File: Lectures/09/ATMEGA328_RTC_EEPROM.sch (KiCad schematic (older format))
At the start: 19 parts, among them U1 ATmega328P-AU, U2 24LC1025, U3 24LC1025, U4 DS1337S+, Y1 Crystal 16MHz, Y2 Crystal 32MHz

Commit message: Included decoupling capacitors
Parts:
- added C10, C4, C5, C6, C7, C8, C9: 100nF, Capacitor_SMD:C_0603_1608Metric_Pad1.08x0.95mm_HandSolder, symbol Device:C
- C1, C2: footprint Capacitor_SMD:C_0805_2012Metric_Pad1.18x1.45mm_HandSolder -> Capacitor_SMD:C_0603_1608Metric_Pad1.08x0.95mm_HandSolder
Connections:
- net labels removed: GNDPWR
- wire segments 107 -> 125
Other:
- moved on the sheet: BT1, C1, C2, D1, R3, U2, Y1

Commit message: Reverse Input Voltage Polarity Protection
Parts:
- removed D2, D3: D, Diode_SMD:D_0805_2012Metric_Pad1.15x1.40mm_HandSolder, symbol Device:D
- added D2, D3: MBR0520LT, Diode_SMD:D_SOD-123, symbol Diode:MBR0520LT
- added Q1: IRLML6401, Package_TO_SOT_SMD:SOT-23, symbol Transistor_FET:IRLML6401
- BT1: value CR1225 -> CR2032; footprint Battery:Battery_CR1225 -> Battery:BatteryHolder_Keystone_1058_1x2032
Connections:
- wire segments 125 -> 123
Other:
- moved on the sheet: BT1, BT2, C3
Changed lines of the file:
@@
 $EndDescr
-$Comp
-L Device:Battery BT2
-U 1 1 60094422
-P 10500 2800
-F 0 "BT2" H 10608 2846 50  0000 L CNN
-F 1 "3.3V" H 10608 2755 50  0000 L CNN
-F 2 "Connector_PinHeader_2.54mm:PinHeader_1x02_P2.54mm_Vertical" V 10500 2860 50  0001 C CNN
-F 3 "~" V 10500 2860 50  0001 C CNN
-	1    10500 2800
-	1    0    0    -1
-$EndComp
-$Comp
-L Device:CP C3
-U 1 1 60096B17
-P 9750 2850
-F 0 "C3" H 9868 2896 50  0000 L CNN
-F 1 "10uF" H 9868 2805 50  0000 L CNN
-F 2 "Capacitor_SMD:C_0805_2012Metric_Pad1.18x1.45mm_HandSolder" H 9788 2700 50  0001 C CNN
-F 3 "~" H 9750 2850 50  0001 C CNN
-	1    9750 2850
-	1    0    0    -1
-$EndComp
 $Comp
 L Custom_RTC_Library:DS1337S+_v1 U4
@@
 	1    8000 2925
 	1    0    0    -1
-$EndComp
-$Comp
-L Device:D D2
-U 1 1 600D352F
-P 7750 1600
-F 0 "D2" V 7796 1520 50  0000 R CNN
-F 1 "D" V 7705 1520 50  0000 R CNN
-F 2 "Diode_SMD:D_0805_2012Metric_Pad1.15x1.40mm_HandSolder" H 7750 1600 50  0001 C CNN
-F 3 "~" H 7750 1600 50  0001 C CNN
-	1    7750 1600
-	0    -1   -1   0
-$EndComp
-$Comp
-L Device:D D3
-U 1 1 600D3E15
-P 8250 1600
-F 0 "D3" V 8296 1520 50  0000 R CNN
-F 1 "D" V 8205 1520 50  0000 R CNN
-F 2 "Diode_SMD:D_0805_2012Metric_Pad1.15x1.40mm_HandSolder" H 8250 1600 50  0001 C CNN
-F 3 "~" H 8250 1600 50  0001 C CNN
-	1    8250 1600
-	0    -1   -1   0
 $EndComp
 Text Label 8750 4600 2    50   ~ 0
@@
 	8750 5750 9000 5750
 Wire Wire Line
-	8750 5875 8875 5875
-Wire Wire Line
-	8875 6000 8875 5875
-Connection ~ 8875 5875
-Wire Wire Line
-	8875 5875 9000 5875
-Wire Wire Line
 	10250 4600 10500 4600
 Wire Wire Line
@@
 Wire Wire Line
 	8600 3175 8750 3175
-Text Label 7750 1250 0    50   ~ 0
+Text Label 7625 1250 0    50   ~ 0
 Vcc
 $Comp
 L Device:Battery_Cell BT1
 U 1 1 600D5613
-P 8750 1450
-F 0 "BT1" H 8868 1546 50  0000 L CNN
-F 1 "CR1225" H 8868 1455 50  0000 L CNN
-F 2 "Battery:Battery_CR1225" V 8750 1510 50  0001 C CNN
-F 3 "~" V 8750 1510 50  0001 C CNN
-	1    8750 1450
-	1    0    0    -1
-$EndComp
-Wire Wire Line
-	7750 1750 7750 1850
-Wire Wire Line
-	8250 1750 8250 1850
-Wire Wire Line
-	7750 1250 7750 1450
-Wire Wire Line
-	8250 1450 8250 1250
-Wire Wire Line
-	8250 1250 8750 1250
-Wire Wire Line
-	8750 1750 8750 1550
+P 8750 1525
+F 0 "BT1" H 8868 1621 50  0000 L CNN
+F 1 "CR2032" H 8868 1530 50  0000 L CNN
+F 2 "Battery:BatteryHolder_Keystone_1058_1x2032" V 8750 1585 50  0001 C CNN
+F 3 "~" V 8750 1585 50  0001 C CNN
+	1    8750 1525
+	1    0    0    -1
+$EndComp
 $Comp
 L Memory_EEPROM:24LC1025 U3
@@
 Wire Wire Line
 	5550 2550 5550 2500
-Wire Wire Line
-	9750 3000 9750 3125
-Wire Wire Line
-	10500 3125 10500 3000
-Text Label 10125 2250 0    50   ~ 0
+Text Label 6075 5750 0    50   ~ 0
 Vcc
-Wire Wire Line
-	9750 2700 9750 2500
-Wire Wire Line
-	9750 2500 10125 2500
-Wire Wire Line
-	10500 2500 10500 2600
-Wire Wire Line
-	10125 2250 10125 2375
-Connection ~ 10125 2500
-Wire Wire Line
-	10125 2500 10500 2500
 $Comp
 L Device:LED D1
@@
 NoConn ~ 2400 3475
 NoConn ~ 2400 3575
-$Comp
-L power:PWR_FLAG #FLG0101
-U 1 1 601BAE2E
-P 10125 2375
-F 0 "#FLG0101" H 10125 2450 50  0001 C CNN
-F 1 "PWR_FLAG" V 10125 2503 50  0000 L CNN
-F 2 "" H 10125 2375 50  0001 C CNN
-F 3 "~" H 10125 2375 50  0001 C CNN
-	1    10125 2375
-	0    1    1    0
-$EndComp
-Connection ~ 10125 2375
-Wire Wire Line
-	10125 2375 10125 2500
 Wire Notes Line
 	4750 1000 6250 1000
 Wire Notes Line
 	6500 1000 9250 1000
-Wire Notes Line
-	9500 1000 11000 1000
 Text Notes 6500 975  0    50   ~ 0
 N3 - Clock/Calendar and Backup Battery
@@
 Text Notes 625  975  0    50   ~ 0
 N1 - Atmega328P with Oscillator
-Text Notes 9500 975  0    50   ~ 0
+Text Notes 4750 5225 0    50   ~ 0
 N4 - External Battery Terminal
 Wire Notes Line
 	6500 4000 9250 4000
 Wire Notes Line
-	9500 4000 11000 4000
-Wire Notes Line
 	6500 4000 6500 1000
 Wire Notes Line
 	9250 1000 9250 4000
-Wire Notes Line
-	9500 4000 9500 1000
-Wire Notes Line
-	11000 1000 11000 4000
 Wire Notes Line
 	8250 4250 8250 6250
@@
 $EndComp
 $Comp
-L power:GND #PWR014
-U 1 1 600D5E04
-P 8875 6000
-F 0 "#PWR014" H 8875 5750 50  0001 C CNN
-F 1 "GND" H 8880 5827 50  0000 C CNN
-F 2 "" H 8875 6000 50  0001 C CNN
-F 3 "" H 8875 6000 50  0001 C CNN
-	1    8875 6000
-	1    0    0    -1
-$EndComp
-$Comp
 L power:GND #PWR015
 U 1 1 600D67BE
-P 10125 3325
-F 0 "#PWR015" H 10125 3075 50  0001 C CNN
-F 1 "GND" H 10130 3152 50  0000 C CNN
-F 2 "" H 10125 3325 50  0001 C CNN
-F 3 "" H 10125 3325 50  0001 C CNN
-	1    10125 3325
+P 5000 6325
+F 0 "#PWR015" H 5000 6075 50  0001 C CNN
+F 1 "GND" H 5005 6152 50  0000 C CNN
+F 2 "" H 5000 6325 50  0001 C CNN
+F 3 "" H 5000 6325 50  0001 C CNN
+	1    5000 6325
 	1    0    0    -1
 $EndComp
@@
 L power:GND #PWR013
 U 1 1 600D7A06
-P 8750 1750
-F 0 "#PWR013" H 8750 1500 50  0001 C CNN
-F 1 "GND" H 8755 1577 50  0000 C CNN
-F 2 "" H 8750 1750 50  0001 C CNN
-F 3 "" H 8750 1750 50  0001 C CNN
-	1    8750 1750
+P 8750 1725
+F 0 "#PWR013" H 8750 1475 50  0001 C CNN
+F 1 "GND" H 8755 1552 50  0000 C CNN
+F 2 "" H 8750 1725 50  0001 C CNN
+F 3 "" H 8750 1725 50  0001 C CNN
+	1    8750 1725
 	1    0    0    -1
 $EndComp
@@
 	1    0    0    -1
 $EndComp
-Text Label 10225 3225 0    50   ~ 0
+Text Label 6075 6250 0    50   ~ 0
 GND
-Wire Wire Line
-	9750 3125 10125 3125
-Wire Wire Line
-	10125 3225 10125 3125
-Wire Wire Line
-	10125 3225 10225 3225
-Connection ~ 10125 3125
-Wire Wire Line
-	10125 3125 10500 3125
-Wire Wire Line
-	10125 3325 10125 3225
-Connection ~ 10125 3225
 $Comp
 L power:GND #PWR07
@@
 Text Label 5550 3250 0    50   ~ 0
 Vcc
-Wire Wire Line
-	7750 1850 8000 1850
 $Comp
 L Device:C C10
@@
 Wire Wire Line
 	8000 2325 8000 2175
-Connection ~ 8000 1850
-Wire Wire Line
-	8000 1850 8250 1850
 Wire Wire Line
 	7900 2175 8000 2175
@@
 Wire Notes Line
 	4750 1000 4750 5000
+Wire Wire Line
+	7625 1850 8000 1850
+Wire Wire Line
+	8000 1850 8375 1850
+Connection ~ 8000 1850
+Wire Wire Line
+	8375 1450 8375 1250
+Wire Wire Line
+	8375 1250 8750 1250
+Wire Wire Line
+	8750 1250 8750 1325
+Wire Wire Line
+	8750 1725 8750 1625
+$Comp
+L Diode:MBR0520LT D3
+U 1 1 600C40F8
+P 8375 1600
+F 0 "D3" V 8400 1925 50  0000 R CNN
+F 1 "MBR0520LT" V 8325 2100 50  0000 R CNN
+F 2 "Diode_SMD:D_SOD-123" H 8375 1425 50  0001 C CNN
+F 3 "http://www.onsemi.com/pub_link/Collateral/MBR0520LT1-D.PDF" H 8375 1600 50  0001 C CNN
+	1    8375 1600
+	0    -1   -1   0
+$EndComp
+Wire Wire Line
+	8375 1850 8375 1750
+$Comp
+L Diode:MBR0520LT D2
+U 1 1 600AFB22
+P 7625 1600
+F 0 "D2" V 7650 1925 50  0000 R CNN
+F 1 "MBR0520LT" V 7575 2100 50  0000 R CNN
+F 2 "Diode_SMD:D_SOD-123" H 7625 1425 50  0001 C CNN
+F 3 "http://www.onsemi.com/pub_link/Collateral/MBR0520LT1-D.PDF" H 7625 1600 50  0001 C CNN
+	1    7625 1600
+	0    -1   -1   0
+$EndComp
+Wire Wire Line
+	7625 1450 7625 1250
+Wire Wire Line
+	7625 1850 7625 1750
+Wire Wire Line
+	8750 5875 9000 5875
+$Comp
+L Transistor_FET:IRLML6401 Q1
+U 1 1 600E5C2A
+P 5500 5850
+F 0 "Q1" V 5842 5850 50  0000 C CNN
+F 1 "IRLML6401" V 5751 5850 50  0000 C CNN
+F 2 "Package_TO_SOT_SMD:SOT-23" H 5700 5775 50  0001 L CIN
+F 3 "https://www.infineon.com/dgdl/irlml6401pbf.pdf?fileId=5546d462533600a401535668b96d2634" H 5500 5850 50  0001 L CNN
+	1    5500 5850
+	0    -1   -1   0
+$EndComp
+$Comp
+L Device:Battery BT2
+U 1 1 60094422
+P 5000 5950
+F 0 "BT2" H 5108 5996 50  0000 L CNN
+F 1 "3.3V" H 5108 5905 50  0000 L CNN
+F 2 "Connector_PinHeader_2.54mm:PinHeader_1x02_P2.54mm_Vertical" V 5000 6010 50  0001 C CNN
+F 3 "~" V 5000 6010 50  0001 C CNN
+	1    5000 5950
+	1    0    0    -1
+$EndComp
+$Comp
+L power:PWR_FLAG #FLG0101
+U 1 1 601BAE2E
+P 6000 5825
+F 0 "#FLG0101" H 6000 5900 50  0001 C CNN
+F 1 "PWR_FLAG" V 6000 5953 50  0000 L CNN
+F 2 "" H 6000 5825 50  0001 C CNN
+F 3 "~" H 6000 5825 50  0001 C CNN
+	1    6000 5825
+	0    1    1    0
+$EndComp
+Wire Wire Line
+	5300 5750 5000 5750
+$Comp
+L Device:CP C3
+U 1 1 60096B17
+P 6000 6025
+F 0 "C3" H 6118 6071 50  0000 L CNN
+F 1 "10uF" H 6118 5980 50  0000 L CNN
+F 2 "Capacitor_SMD:C_0805_2012Metric_Pad1.18x1.45mm_HandSolder" H 6038 5875 50  0001 C CNN
+F 3 "~" H 6000 6025 50  0001 C CNN
+	1    6000 6025
+	1    0    0    -1
+$EndComp
+Wire Wire Line
+	5000 6150 5000 6250
+Wire Wire Line
+	5000 6250 5500 6250
+Wire Wire Line
+	5500 6050 5500 6250
+Connection ~ 5500 6250
+Wire Wire Line
+	5000 6325 5000 6250
+Connection ~ 5000 6250
+Wire Wire Line
+	5700 5750 6000 5750
+Wire Wire Line
+	5500 6250 6000 6250
+Wire Wire Line
+	6000 6175 6000 6250
+Connection ~ 6000 6250
+Wire Wire Line
+	6000 6250 6075 6250
+Wire Wire Line
+	6000 5875 6000 5825
+Connection ~ 6000 5750
+Wire Wire Line
+	6000 5750 6075 5750
+Connection ~ 6000 5825
+Wire Wire Line
+	6000 5825 6000 5750
+Wire Notes Line
+	4750 5250 4750 6750
+Wire Notes Line
+	4750 6750 6750 6750
+Wire Notes Line
+	6750 6750 6750 5250
+Wire Notes Line
+	6750 5250 4750 5250
 $EndSCHEMATC

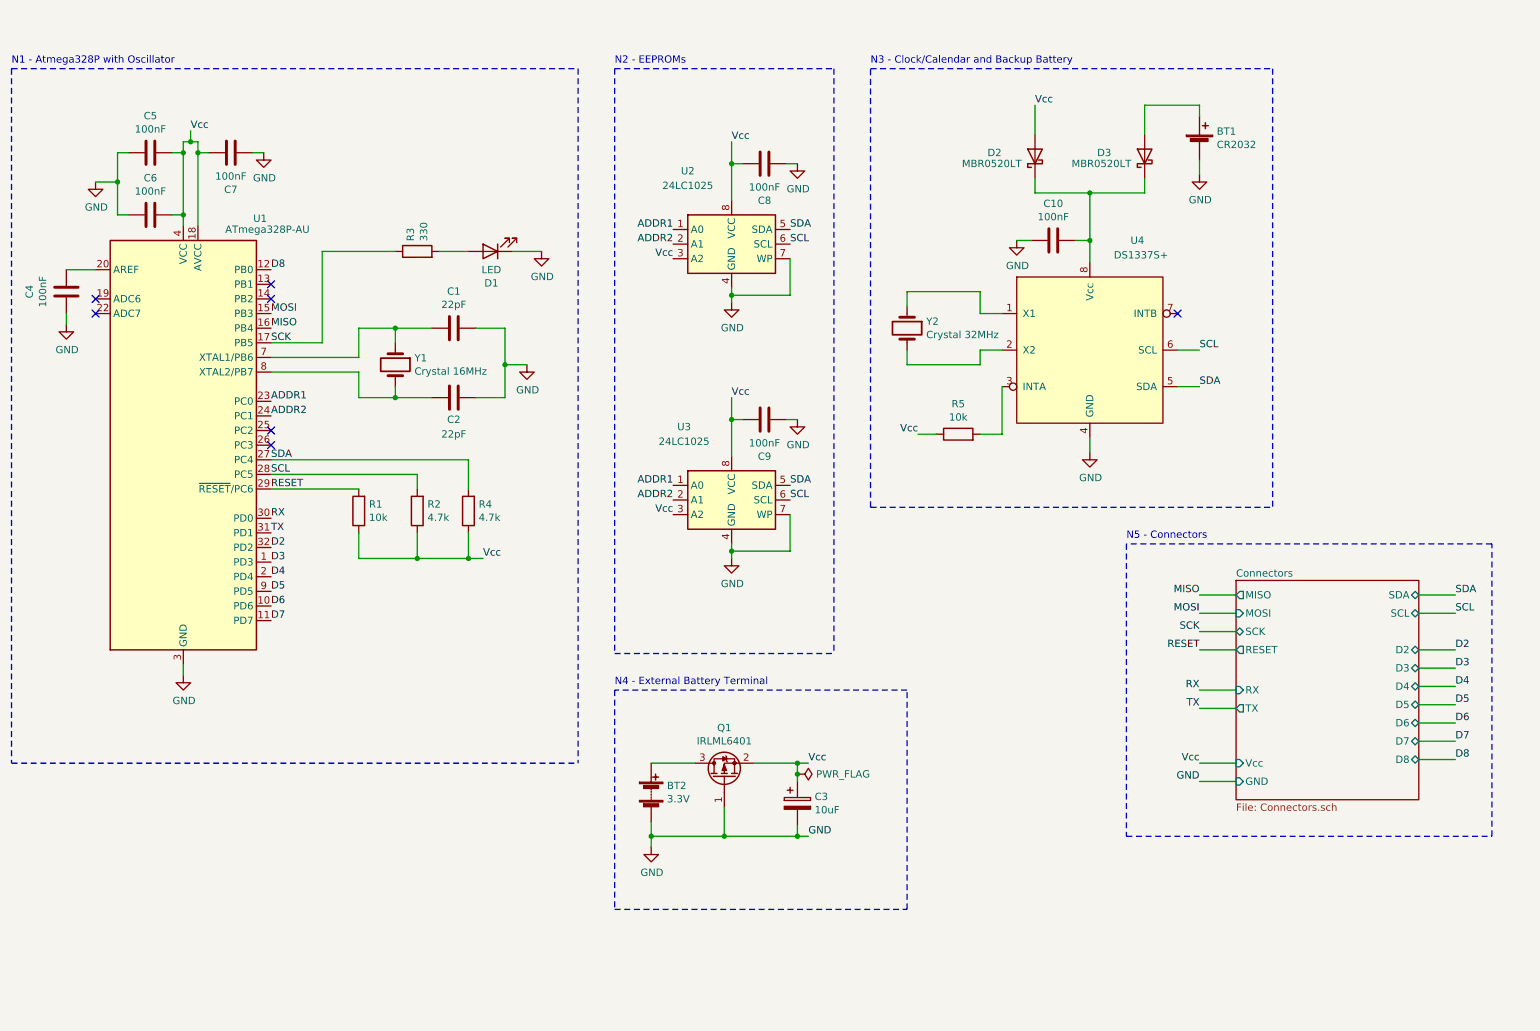
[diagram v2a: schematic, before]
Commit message: Schematic updates
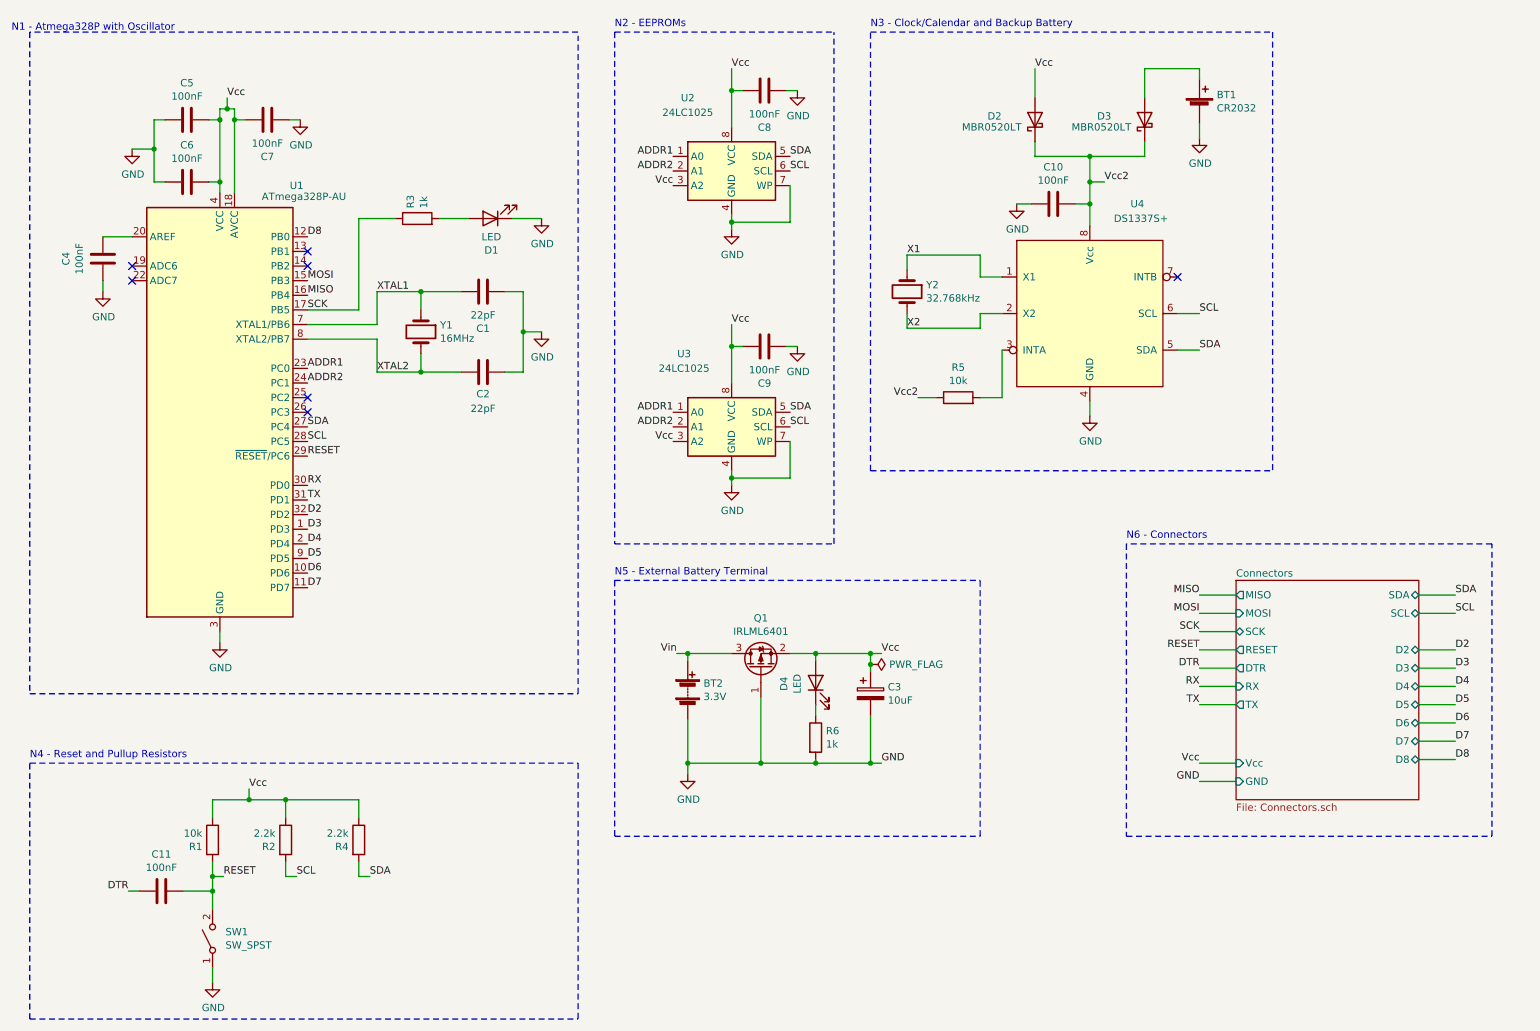
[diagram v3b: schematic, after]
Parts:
- added C11: 100nF, Capacitor_SMD:C_0603_1608Metric, symbol Device:C
- added D4: LED, LED_SMD:LED_0805_2012Metric, symbol Device:LED
- added R6: 1k, Resistor_SMD:R_0805_2012Metric, symbol Device:R
- added SW1: SW_SPST, Button_Switch_SMD:SW_SPST_PTS645, symbol Switch:SW_SPST
- BT2: footprint Connector_PinHeader_2.54mm:PinHeader_1x02_P2.54mm_Vertical -> Connector_PinSocket_2.54mm:PinSocket_1x02_P2.54mm_Vertical
- C1, C2, C4, C5, C6, C7: footprint Capacitor_SMD:C_0603_1608Metric_Pad1.08x0.95mm_HandSolder -> Capacitor_SMD:C_0402_1005Metric
- C10, C8, C9: footprint Capacitor_SMD:C_0603_1608Metric_Pad1.08x0.95mm_HandSolder -> Capacitor_SMD:C_0603_1608Metric
- C3: footprint Capacitor_SMD:C_0805_2012Metric_Pad1.18x1.45mm_HandSolder -> Capacitor_SMD:C_0805_2012Metric
- D1: footprint LED_SMD:LED_0805_2012Metric_Pad1.15x1.40mm_HandSolder -> LED_SMD:LED_0805_2012Metric
- R1, R5: footprint Resistor_SMD:R_0805_2012Metric_Pad1.20x1.40mm_HandSolder -> Resistor_SMD:R_0805_2012Metric
- R2, R4: value 4.7k -> 2.2k; footprint Resistor_SMD:R_0805_2012Metric_Pad1.20x1.40mm_HandSolder -> Resistor_SMD:R_0805_2012Metric
- R3: value 330 -> 1k; footprint Resistor_SMD:R_0805_2012Metric_Pad1.20x1.40mm_HandSolder -> Resistor_SMD:R_0805_2012Metric
- Y1: value Crystal 16MHz -> 16MHz; footprint Crystal:Crystal_SMD_5032-2Pin_5.0x3.2mm_HandSoldering -> Crystal:Crystal_SMD_5032-2Pin_5.0x3.2mm
- Y2: value Crystal 32MHz -> 32.768kHz
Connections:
- net GND: now also C1.2, R6.2, SW1.1 (A); no longer C1.1
- net RESET: now also C11.1, SW1.2 (B)
- net Vcc: now also D4.2 (A); no longer R5.1
- net Vin: now reaches BT2.1 (+), Q1.3 (D)
- net XTAL2: now reaches C2.1, U1.8 (XTAL2/PB7), Y1.2
- net XTAL1: now reaches U1.7 (XTAL1/PB6), Y1.1
- net XTAL1: now also C1.1; no longer C1.2
- net X1: now reaches U4.1 (X1), Y2.1
- net X2: now reaches U4.2 (X2), Y2.2
- net Vcc2: now reaches C10.1, D2.1 (K), D3.1 (K), U4.8 (Vcc)
- net Vcc2: now also R5.1
- new net: D4.1 (K), R6.1
- new net DTR: C11.2
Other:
- note added: "N4 - Reset and Pullup Resistors"
- note added: "N5 - External Battery Terminal"
- note added: "N6 - Connectors"
- note removed: "N4 - External Battery Terminal"
- note removed: "N5 - Connectors"
- moved on the sheet: BT1, BT2, C1, C10, C2, C3, C4, C5, C6, C7, C8, C9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

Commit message: RTC loading capacitors
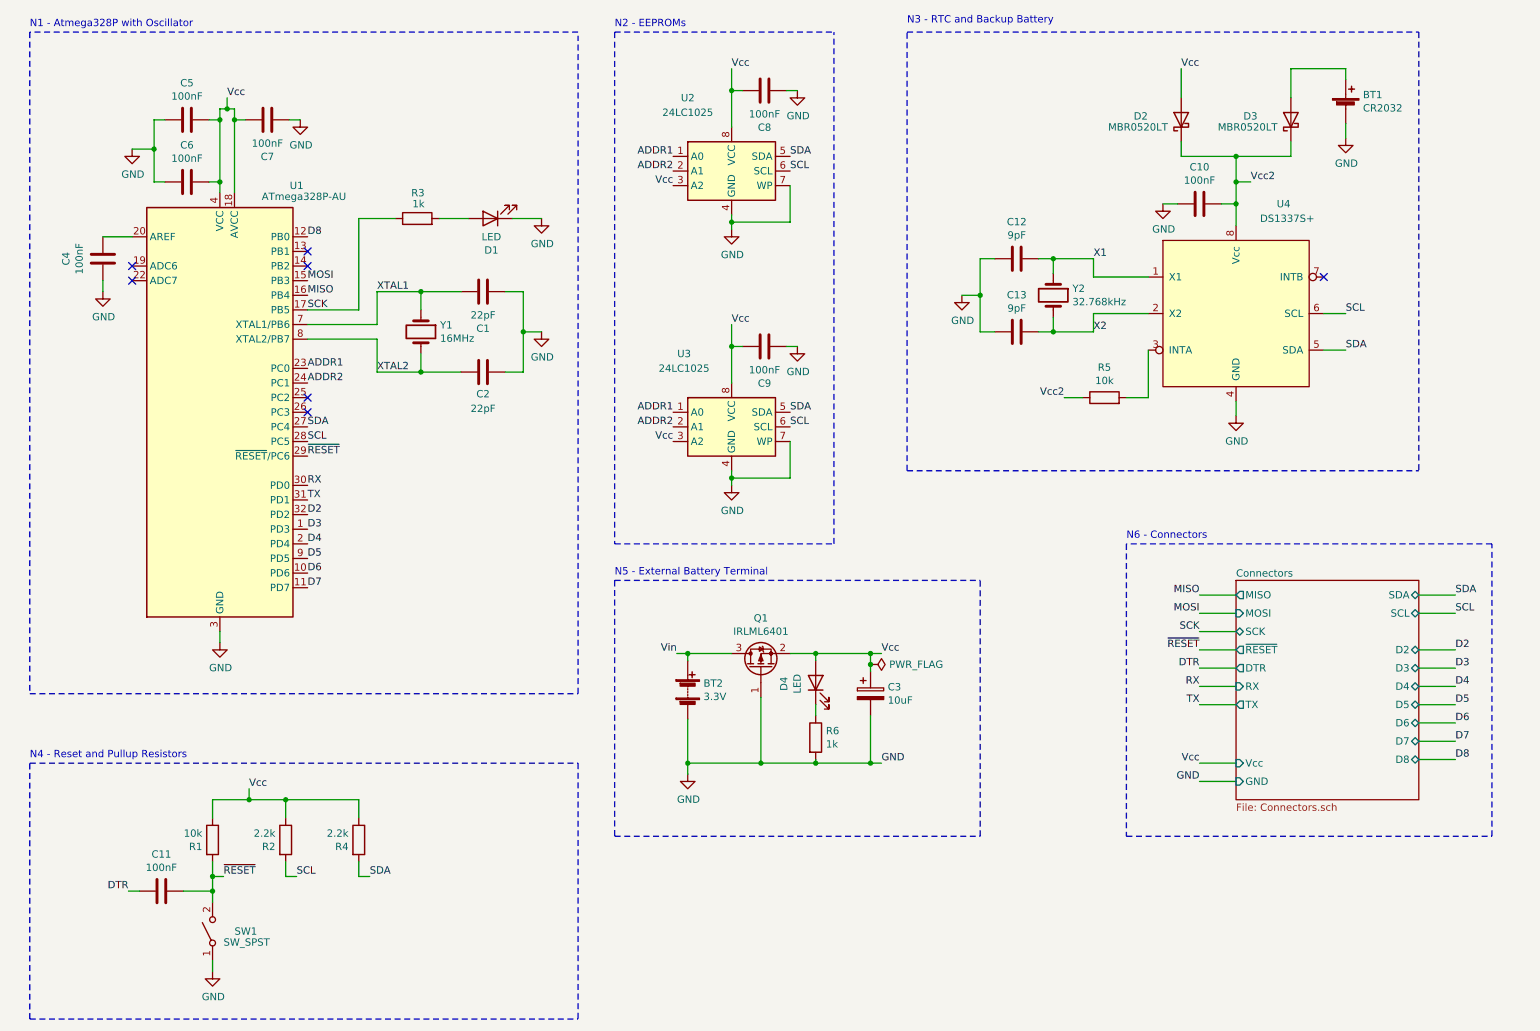
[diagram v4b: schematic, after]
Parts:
- added C12, C13: 9pF, Capacitor_SMD:C_0603_1608Metric, symbol Device:C
- C1, C2, C4, C5, C6, C7: footprint Capacitor_SMD:C_0402_1005Metric -> Capacitor_SMD:C_0603_1608Metric
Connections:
- net GND: now also C12.2, C13.2
- net X1: now also C12.1
- net X2: now also C13.1
- net RESET renamed ~RESET
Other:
- note added: "N3 - RTC and Backup Battery"
- note removed: "N3 - Clock/Calendar and Backup Battery"
- moved on the sheet: BT1, C10, D2, D3, R5, SW1, U4, Y2
